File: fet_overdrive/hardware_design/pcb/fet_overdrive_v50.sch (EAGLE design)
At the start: 32 parts, among them IC1 TL072CD, J1 PJ301_THONKICONN6, J2 PJ301_THONKICONN6, Q1 MMBFJ111, Q2 SMMBT3904LT1G

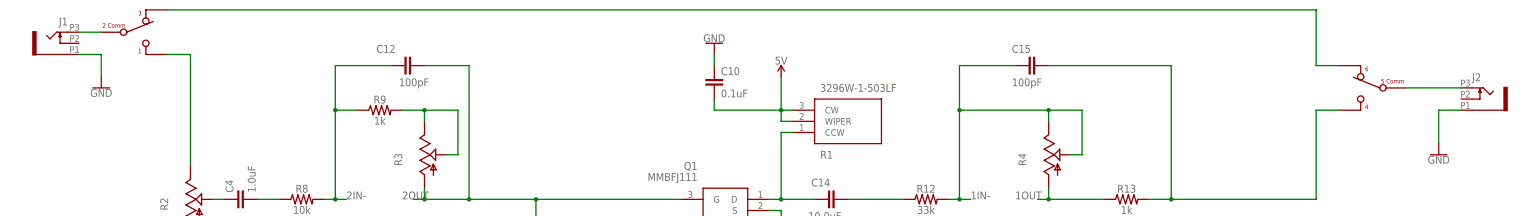
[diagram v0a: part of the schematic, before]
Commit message: progress on audio DAC. switched to f446xx for now
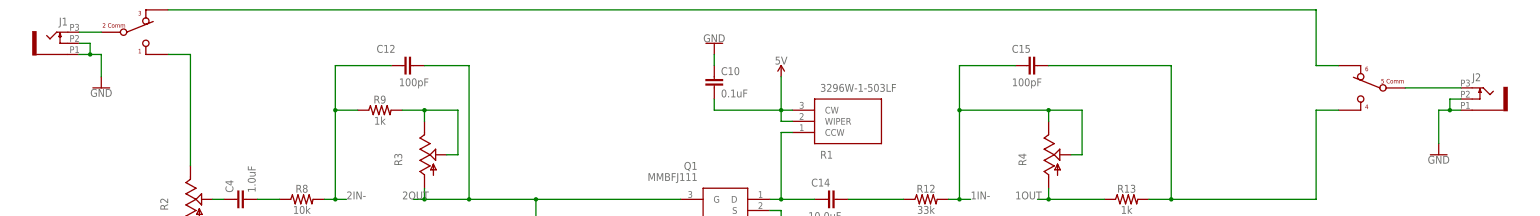
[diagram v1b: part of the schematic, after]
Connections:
- net GND: now also J1.2, J2.2
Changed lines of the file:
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@@
 <segment>
 <pinref part="J1" gate="G$1" pin="1"/>
-<wire x1="38.1" y1="213.36" x2="43.18" y2="213.36" width="0.1524" layer="91"/>
+<wire x1="38.1" y1="213.36" x2="40.64" y2="213.36" width="0.1524" layer="91"/>
+<wire x1="40.64" y1="213.36" x2="43.18" y2="213.36" width="0.1524" layer="91"/>
 <wire x1="43.18" y1="213.36" x2="43.18" y2="208.28" width="0.1524" layer="91"/>
 <pinref part="GND1" gate="1" pin="GND"/>
+<pinref part="J1" gate="G$1" pin="2"/>
+<wire x1="38.1" y1="215.9" x2="40.64" y2="215.9" width="0.1524" layer="91"/>
+<wire x1="40.64" y1="215.9" x2="40.64" y2="213.36" width="0.1524" layer="91"/>
+<junction x="40.64" y="213.36"/>
 </segment>
 <segment>
 <pinref part="J2" gate="G$1" pin="1"/>
-<wire x1="353.06" y1="200.66" x2="347.98" y2="200.66" width="0.1524" layer="91"/>
+<wire x1="353.06" y1="200.66" x2="350.52" y2="200.66" width="0.1524" layer="91"/>
+<wire x1="350.52" y1="200.66" x2="347.98" y2="200.66" width="0.1524" layer="91"/>
 <wire x1="347.98" y1="200.66" x2="347.98" y2="193.04" width="0.1524" layer="91"/>
 <pinref part="GND2" gate="1" pin="GND"/>
+<pinref part="J2" gate="G$1" pin="2"/>
+<wire x1="353.06" y1="203.2" x2="350.52" y2="203.2" width="0.1524" layer="91"/>
+<wire x1="350.52" y1="203.2" x2="350.52" y2="200.66" width="0.1524" layer="91"/>
+<junction x="350.52" y="200.66"/>
 </segment>
 <segment>
